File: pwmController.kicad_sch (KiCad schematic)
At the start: 45 parts, among them J1 RJ12, J14 inputs, J16 relays, J17 relays, J2 Conn_01x08_Male, J3 Conn_01x08_Male, J4 Conn_01x08_Male, J5 power, J6 gnd, J7 inputs, J8 track out, K1 G5V-1, K2 G5V-1, K3 G5V-1, K4 G5V-1, K5 G5V-1, K6 G5V-1, K7 G5V-1, K8 G5V-1, U1 24LC256, U2 MAX485E, U3 L298N, U5 ULN2803A, U7 Buck

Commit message: may have the relays working. Should be tested with an LED as soon as the IO extender arrives. Also need to solder pin1 (A0) to 5V due to address conflict with mcp23017
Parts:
- U4: value (none) -> MCP23017_SP; footprint (none) -> Package_DIP:DIP-28_W7.62mm
- U6: value (none) -> PCF8574; footprint (none) -> Package_DIP:DIP-16_W7.62mm_Socket
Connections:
- net +5V: now also U6.1 (A0)
- net GND: no longer U6.1 (A0)
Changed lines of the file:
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@@
   (junction (at 386.08 21.59) (diameter 0) (color 0 0 0 0)
   )
+  (junction (at 250.19 38.1) (diameter 0) (color 0 0 0 0)
+  )
   (junction (at 361.95 160.02) (diameter 0) (color 0 0 0 0)
   )
@@
   )
   (junction (at 71.12 167.64) (diameter 0) (color 0 0 0 0)
-  )
-  (junction (at 232.41 55.88) (diameter 0) (color 0 0 0 0)
   )
   (junction (at 83.82 181.61) (diameter 0) (color 0 0 0 0)
@@
     (stroke (width 0) (type default) (color 0 0 0 0))
   )
+  (wire (pts (xy 232.41 53.34) (xy 232.41 38.1))
+    (stroke (width 0) (type default) (color 0 0 0 0))
+  )
   (wire (pts (xy 35.56 78.74) (xy 40.64 78.74))
     (stroke (width 0) (type default) (color 0 0 0 0))
@@
     (stroke (width 0) (type default) (color 0 0 0 0))
   )
+  (wire (pts (xy 237.49 53.34) (xy 232.41 53.34))
+    (stroke (width 0) (type default) (color 0 0 0 0))
+  )
   (wire (pts (xy 19.05 20.32) (xy 40.64 20.32))
     (stroke (width 0) (type default) (color 0 0 0 0))
@@
     (stroke (width 0) (type default) (color 0 0 0 0))
   )
+  (wire (pts (xy 232.41 38.1) (xy 250.19 38.1))
+    (stroke (width 0) (type default) (color 0 0 0 0))
+  )
   (wire (pts (xy 262.89 53.34) (xy 275.59 53.34))
     (stroke (width 0) (type default) (color 0 0 0 0))
@@
     (stroke (width 0) (type default) (color 0 0 0 0))
   )
-  (wire (pts (xy 232.41 53.34) (xy 232.41 55.88))
-    (stroke (width 0) (type default) (color 0 0 0 0))
-  )
   (wire (pts (xy 167.64 59.69) (xy 167.64 68.58))
     (stroke (width 0) (type default) (color 0 0 0 0))
@@
   )
   (wire (pts (xy 350.52 170.18) (xy 364.49 170.18))
-    (stroke (width 0) (type default) (color 0 0 0 0))
-  )
-  (wire (pts (xy 237.49 53.34) (xy 232.41 53.34))
     (stroke (width 0) (type default) (color 0 0 0 0))
   )
@@
       (effects (font (size 1.27 1.27)) (justify left))
     )
-    (property "Value" "" (id 1) (at 252.2094 39.4771 0)
-      (effects (font (size 1.27 1.27)) (justify left))
-    )
-    (property "Footprint" "" (id 2) (at 250.19 55.88 0)
+    (property "Value" "PCF8574" (id 1) (at 252.2094 39.4771 0)
+      (effects (font (size 1.27 1.27)) (justify left))
+    )
+    (property "Footprint" "Package_DIP:DIP-16_W7.62mm_Socket" (id 2) (at 250.19 55.88 0)
       (effects (font (size 1.27 1.27)) hide)
     )
@@
       (effects (font (size 1.27 1.27)) (justify left))
     )
-    (property "Value" "" (id 1) (at 235.6994 -59.5829 0)
-      (effects (font (size 1.27 1.27)) (justify left))
-    )
-    (property "Footprint" "" (id 2) (at 238.76 -10.16 0)
+    (property "Value" "MCP23017_SP" (id 1) (at 235.6994 -59.5829 0)
+      (effects (font (size 1.27 1.27)) (justify left))
+    )
+    (property "Footprint" "Package_DIP:DIP-28_W7.62mm" (id 2) (at 238.76 -10.16 0)
       (effects (font (size 1.27 1.27)) (justify left) hide)
     )

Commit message: made drastic changes to PCB design. I added 2nd Rj12 connector, side by side connectors, 2 analog inpouts and 2nd channel of H bridge is commissioned
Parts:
- removed J8: track out, TerminalBlock_Phoenix:TerminalBlock_Phoenix_MKDS-1,5-2-5.08_1x02_P5.08mm_Horizontal, symbol Connector:Screw_Terminal_01x02
- removed JP2, JP4: jmp, Jumper:SolderJumper-2_P1.3mm_Open_RoundedPad1.0x1.5mm, symbol Jumper:SolderJumper_2_Open
- added C8, C9: 100nF, Capacitor_THT:C_Disc_D3.0mm_W1.6mm_P2.50mm, symbol Device:C
- added D1, D10, D8, D9: D, Diode_THT:D_DO-34_SOD68_P7.62mm_Horizontal, symbol Device:D
- added J10: Conn_01x06_Female, Connector_PinSocket_2.54mm:PinSocket_1x06_P2.54mm_Horizontal, symbol Connector:Conn_01x06_Female
- added J11, J12: track out, TerminalBlock_Phoenix:TerminalBlock_Phoenix_MKDS-1,5-2-5.08_1x02_P5.08mm_Horizontal, symbol Connector:Screw_Terminal_01x02
- added J13, J15: ADC, Connector_PinHeader_2.54mm:PinHeader_1x03_P2.54mm_Vertical, symbol Connector:Conn_01x03_Male
- added J8: Conn_01x06_Male, Connector_PinHeader_2.54mm:PinHeader_1x06_P2.54mm_Horizontal, symbol Connector:Conn_01x06_Male
- added J9: RJ12, Connector_RJ:RJ12_Amphenol_54601, symbol Connector:RJ12
- added R1: R, Resistor_THT:R_Axial_DIN0516_L15.5mm_D5.0mm_P20.32mm_Horizontal, symbol Device:R
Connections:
- net +12V: now also D3.1 (K), D5.1 (K), D1.1 (K), D9.1 (K), J10.5 (Pin_5), J10.6 (Pin_6), J8.5 (Pin_5), J8.6 (Pin_6), J9.5; no longer D2.1 (K), D4.1 (K), D7.1 (K), U7.4 (in+)
- net +5V: now also U3.11 (EnB), C8.1, C9.1, J13.2 (Pin_2), J15.2 (Pin_2)
- net GND: now also D2.2 (A), D4.2 (A), R2.1, D10.2 (A), D8.2 (A), J10.1 (Pin_1), J10.2 (Pin_2), J13.1 (Pin_1), J15.1 (Pin_1), J8.1 (Pin_1), J8.2 (Pin_2), J9.2, R1.2; no longer D3.2 (A), D5.2 (A), R2.2
- net pwm1: now also A1.13 (D10); no longer A1.19 (A0)
- net pwm2: now also A1.12 (D9); no longer A1.20 (A1)
- net servo7: now also A1.19 (A0); no longer A1.12 (D9)
- net servo8: now also A1.20 (A1); no longer A1.13 (D10)
- net pwm3: now reaches A1.14 (D11)
- net pwm3: now also U3.12 (IN4)
- net pwm4: now reaches A1.15 (D12)
- net pwm4: now also U3.10 (IN3)
- net ADC2: now reaches A1.22 (A3)
- net ADC2: now also C9.2, J13.3 (Pin_3)
- net CS1: now reaches A1.25 (A6)
- net CS1: now also R2.2, U3.1 (SENSE_A)
- net CS2: now reaches A1.26 (A7)
- net CS2: now also U3.15 (SENSE_B), R1.1
- net B: now reaches J1.3, U2.7 (B)
- net B: now also J10.3 (Pin_3), J8.3 (Pin_3), J9.3
- net A: now reaches J1.4, U2.6 (A)
- net A: now also J10.4 (Pin_4), J8.4 (Pin_4), J9.4
- net track2R: now reaches U3.13 (OUT3)
- net track2R: now also D3.2 (A), D4.1 (K), J12.2 (Pin_2)
- net track2L: now reaches U3.14 (OUT4)
- net track2L: now also D10.1 (K), D9.2 (A), J12.1 (Pin_1)
- net coil1_: no longer names the net of U5.8 (I8)
- net coil1_: now also U6.12 (P7); no longer U6.9 (P4)
- net coil2_: no longer names the net of U6.10 (P5)
- net coil2_: now also U5.6 (I6); no longer U5.7 (I7)
- net coil3_: no longer names the net of U6.11 (P6)
- net coil3_: now also U5.7 (I7); no longer U5.6 (I6)
- net coil4_: no longer names the net of U5.5 (I5)
- net coil4_: now also U6.9 (P4); no longer U6.12 (P7)
- net coil5_: no longer names the net of U5.4 (I4), U6.7 (P3)
- net coil6_: no longer names the net of U5.3 (I3), U6.6 (P2)
- net coil7_: no longer names the net of U5.2 (I2), U6.5 (P1)
- net coil8_: no longer names the net of U5.1 (I1), U6.4 (P0)
- net overcurrent renamed ADC1
- net ADC1: now also C8.2, J15.3 (Pin_3)
- removed net rightTrack: D2.2 (A), D3.1 (K), U3.3 (OUT2)
- new net: D7.1 (K), U7.4 (in+)
- new net track1L: D5.2 (A), D8.1 (K), J11.1 (Pin_1), U3.3 (OUT2)
- new net track1R: D1.2 (A), D2.1 (K), J11.2 (Pin_2), U3.2 (OUT1)
- no-connect marks 24 -> 20
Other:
- added sheet EEPROM (EEPROM.kicad_sch)
- added sheet GPIO (GPIO.kicad_sch)
- added sheet H-bridge (H-brigde.kicad_sch)
- added sheet Inputs (Inputs.kicad_sch)
- added sheet interface (interface.kicad_sch)
- added sheet power (power.kicad_sch)
- added sheet relays (relays.kicad_sch)
- added sheet uController (uController.kicad_sch)
- moved on the sheet: C1, C2, C3, C4, C5, C6, C7, D6, D7, J1, J14, J16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

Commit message: divided the schematic in several sheets.
PCB needs to be redrawn because the link between components is gone
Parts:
- removed A1: Arduino_Nano_v3.x, Module:Arduino_Nano, symbol MCU_Module:Arduino_Nano_v3.x
- removed C1, C2, C3, C4, C5, C8, C9: 100nF, Capacitor_THT:C_Disc_D3.0mm_W1.6mm_P2.50mm, symbol Device:C
- removed C6, C7: CP, Capacitor_THT:CP_Radial_D8.0mm_P3.50mm, symbol Device:C_Polarized
- removed D1, D10, D2, D3, D4, D5, D6, D7, D8, D9: D, Diode_THT:D_DO-34_SOD68_P7.62mm_Horizontal, symbol Device:D
- removed J1, J9: RJ12, Connector_RJ:RJ12_Amphenol_54601, symbol Connector:RJ12
- removed J10: Conn_01x06_Female, Connector_PinSocket_2.54mm:PinSocket_1x06_P2.54mm_Horizontal, symbol Connector:Conn_01x06_Female
- removed J11, J12: track out, TerminalBlock_Phoenix:TerminalBlock_Phoenix_MKDS-1,5-2-5.08_1x02_P5.08mm_Horizontal, symbol Connector:Screw_Terminal_01x02
- removed J13, J15: ADC, Connector_PinHeader_2.54mm:PinHeader_1x03_P2.54mm_Vertical, symbol Connector:Conn_01x03_Male
- removed J14, J7: inputs, TerminalBlock_Phoenix:TerminalBlock_Phoenix_MPT-0,5-8-2.54_1x08_P2.54mm_Horizontal, symbol Connector:Screw_Terminal_01x08
- removed J16, J17: relays, TerminalBlock_Phoenix:TerminalBlock_Phoenix_MKDS-1,5-5-5.08_1x05_P5.08mm_Horizontal, symbol Connector:Screw_Terminal_01x05
- removed J2, J3, J4: Conn_01x08_Male, Connector_PinHeader_2.54mm:PinHeader_1x08_P2.54mm_Vertical, symbol Connector:Conn_01x08_Male
- removed J5: power, TerminalBlock_Phoenix:TerminalBlock_Phoenix_MKDS-1,5-2-5.08_1x02_P5.08mm_Horizontal, symbol Connector:Screw_Terminal_01x02
- removed J6: gnd, TerminalBlock_Phoenix:TerminalBlock_Phoenix_MKDS-1,5-2-5.08_1x02_P5.08mm_Horizontal, symbol Connector:Screw_Terminal_01x02
- removed J8: Conn_01x06_Male, Connector_PinHeader_2.54mm:PinHeader_1x06_P2.54mm_Horizontal, symbol Connector:Conn_01x06_Male
- removed JP1, JP3: jmp, Jumper:SolderJumper-2_P1.3mm_Open_RoundedPad1.0x1.5mm, symbol Jumper:SolderJumper_2_Open
- removed K1, K2, K3, K4, K5, K6, K7, K8: G5V-1, Relay_THT:Relay_SPDT_Omron_G5V-1, symbol Relay:G5V-1
- removed R1, R2: R, Resistor_THT:R_Axial_DIN0516_L15.5mm_D5.0mm_P20.32mm_Horizontal, symbol Device:R
- removed U1: 24LC256, Package_DIP:DIP-8_W7.62mm_Socket, symbol Memory_EEPROM:24LC256
- removed U2: MAX485E, Package_DIP:DIP-8_W7.62mm_Socket, symbol Interface_UART:MAX485E
- removed U3: L298N, Package_TO_SOT_THT:TO-220-15_P2.54x2.54mm_StaggerOdd_Lead4.58mm_Vertical, symbol Driver_Motor:L298N
- removed U4: MCP23017_SP, Package_DIP:DIP-28_W7.62mm, symbol Interface_Expansion:MCP23017_SP
- removed U5: ULN2803A, Package_DIP:DIP-18_W7.62mm_Socket, symbol Transistor_Array:ULN2803A
- removed U6: PCF8574, Package_DIP:DIP-16_W7.62mm_Socket, symbol Interface_Expansion:PCF8574
- removed U7: Buck, custom_kicad_lib_sk:Buck, symbol custom_kicad_lib_sk:Buck
- added H1: MountingHole, MountingHole:MountingHole_3.2mm_M3, symbol Mechanical:MountingHole
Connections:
- no-connect marks 20 -> 0
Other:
- title: (none) -> General Purpose IO module

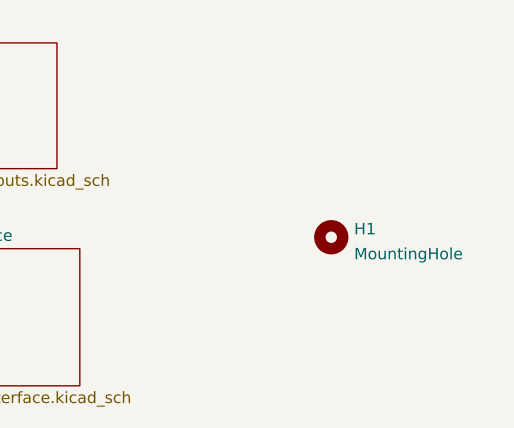
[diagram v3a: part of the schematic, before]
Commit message: changed PCB layout. I want to change more
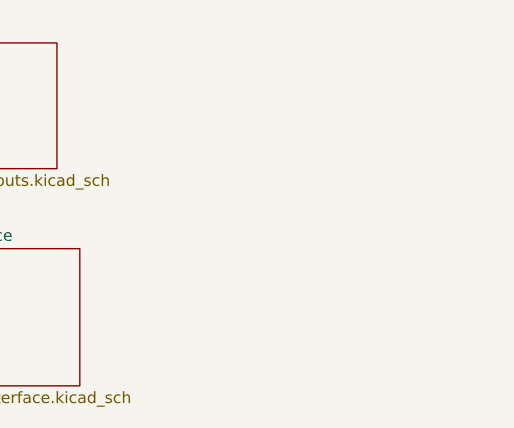
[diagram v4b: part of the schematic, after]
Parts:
- removed H1: MountingHole, MountingHole:MountingHole_3.2mm_M3, symbol Mechanical:MountingHole
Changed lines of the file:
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@@
     (title "General Purpose IO module")
-  )
-  (symbol (lib_id "Mechanical:MountingHole") (at 137.16 40.64 0) (unit 1)
-    (in_bom yes) (on_board yes) (fields_autoplaced)
-    (property "Reference" "H1" (id 0) (at 139.7 39.7315 0)
-      (effects (font (size 1.27 1.27)) (justify left))
-    )
-    (property "Value" "MountingHole" (id 1) (at 139.7 42.5066 0)
-      (effects (font (size 1.27 1.27)) (justify left))
-    )
-    (property "Footprint" "MountingHole:MountingHole_3.2mm_M3" (id 2) (at 137.16 40.64 0)
-      (effects (font (size 1.27 1.27)) hide)
-    )
-    (property "Datasheet" "~" (id 3) (at 137.16 40.64 0)
-      (effects (font (size 1.27 1.27)) hide)
-    )
   )
   (sheet (at 44.45 19.05) (size 15.24 13.97) (fields_autoplaced)
@@
   )
   (symbol_instances
+    (path "/15782add-6e54-4e42-a416-61587f86a435/b3b296ec-345a-438b-88ed-a17ad8ea1576"
+      (reference "#PWR01") (unit 1) (value "+5VA") (footprint "")
+    )
+    (path "/15782add-6e54-4e42-a416-61587f86a435/477facc6-d79a-4dc1-aa3f-86d3bfcca217"
+      (reference "#PWR02") (unit 1) (value "GND") (footprint "")
+    )
+    (path "/15782add-6e54-4e42-a416-61587f86a435/6bf1db2f-8218-4a37-a9ff-28ef9eaeb797"
+      (reference "#PWR03") (unit 1) (value "+5VA") (footprint "")
+    )
+    (path "/15782add-6e54-4e42-a416-61587f86a435/55e2c3cb-7f20-4485-ad3b-1197a660a113"
+      (reference "#PWR04") (unit 1) (value "GND") (footprint "")
+    )
+    (path "/15782add-6e54-4e42-a416-61587f86a435/d1c3fdda-f91d-46b3-8903-4960f9091474"
+      (reference "#PWR05") (unit 1) (value "+5VA") (footprint "")
+    )
+    (path "/15782add-6e54-4e42-a416-61587f86a435/cdb33e69-9124-44b7-8240-f0a2802b2629"
+      (reference "#PWR06") (unit 1) (value "GND") (footprint "")
+    )
+    (path "/15782add-6e54-4e42-a416-61587f86a435/00ee47e2-6951-4070-a450-31f2b1ca61d3"
+      (reference "#PWR07") (unit 1) (value "+5VA") (footprint "")
+    )
+    (path "/15782add-6e54-4e42-a416-61587f86a435/5f987a96-f88c-4c48-9f54-bbb04a7ce0ef"
+      (reference "#PWR08") (unit 1) (value "GND") (footprint "")
+    )
+    (path "/15782add-6e54-4e42-a416-61587f86a435/3acd1d09-7fc9-4a1f-a5a5-37e07d950b90"
+      (reference "#PWR09") (unit 1) (value "+5VA") (footprint "")
+    )
+    (path "/15782add-6e54-4e42-a416-61587f86a435/aefbab52-ffa8-43be-9197-a2369b46f6f8"
+      (reference "#PWR010") (unit 1) (value "GND") (footprint "")
+    )
+    (path "/15782add-6e54-4e42-a416-61587f86a435/6ae46c10-d334-4f3b-8139-fb8860a013fa"
+      (reference "#PWR011") (unit 1) (value "+5VA") (footprint "")
+    )
+    (path "/15782add-6e54-4e42-a416-61587f86a435/78256dce-621e-4a17-8c09-6319ed56b2a8"
+      (reference "#PWR012") (unit 1) (value "GND") (footprint "")
+    )
+    (path "/15782add-6e54-4e42-a416-61587f86a435/c817151f-f542-498d-97f2-d7ebb5b3f4fa"
+      (reference "#PWR013") (unit 1) (value "+5VA") (footprint "")
+    )
+    (path "/15782add-6e54-4e42-a416-61587f86a435/30f5cbe6-e68a-408b-acaf-ef8b43b55fee"
+      (reference "#PWR014") (unit 1) (value "GND") (footprint "")
+    )
+    (path "/15782add-6e54-4e42-a416-61587f86a435/7c34da4a-24eb-4b22-b57e-58032e42e0b1"
+      (reference "#PWR015") (unit 1) (value "+5VA") (footprint "")
+    )
+    (path "/15782add-6e54-4e42-a416-61587f86a435/525a8aee-73cc-4405-b368-88dcce894336"
+      (reference "#PWR016") (unit 1) (value "GND") (footprint "")
+    )
     (path "/5124c4e8-cf6f-404c-8295-c381ef25d08e/8cd7260d-64a2-4a0a-84b1-03181d2c20d1"
       (reference "#PWR0101") (unit 1) (value "GND") (footprint "")
@@
       (reference "#PWR0145") (unit 1) (value "+5V") (footprint "")
     )
-    (path "/15782add-6e54-4e42-a416-61587f86a435/c3c7618f-202a-4b95-b24f-26429b84f4b4"
-      (reference "#PWR0146") (unit 1) (value "GND") (footprint "")
-    )
     (path "/15782add-6e54-4e42-a416-61587f86a435/7a90d089-3f47-41b2-98dc-ed4e9de11862"
       (reference "#PWR0147") (unit 1) (value "GND") (footprint "")
@@
       (reference "#PWR0152") (unit 1) (value "+5V") (footprint "")
     )
-    (path "/15782add-6e54-4e42-a416-61587f86a435/09933ea0-69c3-4150-8976-14f066ab6d37"
-      (reference "#PWR0153") (unit 1) (value "+5VA") (footprint "")
-    )
     (path "/af34ff1d-4916-46f6-b451-19970cdd1d1e/7688b1d7-a5ef-4546-a75a-1dff2b181b93"
       (reference "A1") (unit 1) (value "Arduino_Nano_v3.x") (footprint "Module:Arduino_Nano")
@@
       (reference "D5") (unit 1) (value "D") (footprint "Diode_THT:D_DO-34_SOD68_P7.62mm_Horizontal")
     )
-    (path "/f2e2196a-c83d-497b-b552-0ac27a56ad59/d60723be-0ece-433c-a3cc-8d026e9d4965"
+    (path "/f2e2196a-c83d-497b-b552-0ac27a56ad59/080eb162-2f68-4483-9aa9-cc8e8faf283b"
       (reference "D6") (unit 1) (value "D") (footprint "Diode_THT:D_DO-34_SOD68_P7.62mm_Horizontal")
     )
-    (path "/f2e2196a-c83d-497b-b552-0ac27a56ad59/9f45c2e1-5058-4d3e-94a1-6b3749545d34"
+    (path "/f2e2196a-c83d-497b-b552-0ac27a56ad59/cccb90f6-fcad-4bcc-a6b4-253eb1bab824"
       (reference "D7") (unit 1) (value "D") (footprint "Diode_THT:D_DO-34_SOD68_P7.62mm_Horizontal")
     )
@@
       (reference "D10") (unit 1) (value "D") (footprint "Diode_THT:D_DO-34_SOD68_P7.62mm_Horizontal")
     )
-    (path "/0f730ef4-6b18-4cbd-969a-e0f8ab1030b2"
-      (reference "H1") (unit 1) (value "MountingHole") (footprint "MountingHole:MountingHole_3.2mm_M3")
-    )
     (path "/5124c4e8-cf6f-404c-8295-c381ef25d08e/e63a5e26-dfc1-4721-a4c6-783bbc15c68d"
       (reference "J1") (unit 1) (value "track out") (footprint "TerminalBlock_Phoenix:TerminalBlock_Phoenix_MKDS-1,5-2-5.08_1x02_P5.08mm_Horizontal")
@@
       (reference "J13") (unit 1) (value "ADC") (footprint "Connector_PinHeader_2.54mm:PinHeader_1x03_P2.54mm_Vertical")
     )
-    (path "/15782add-6e54-4e42-a416-61587f86a435/a781526d-7b97-41d9-9f6e-e89d018605de"
-      (reference "J14") (unit 1) (value "Conn_01x08_Male") (footprint "Connector_PinHeader_2.54mm:PinHeader_1x08_P2.54mm_Vertical")
-    )
     (path "/15782add-6e54-4e42-a416-61587f86a435/b24c9c2e-34a1-43da-8250-9a261bf9c0e3"
       (reference "J15") (unit 1) (value "ADC") (footprint "Connector_PinHeader_2.54mm:PinHeader_1x03_P2.54mm_Vertical")
     )
-    (path "/15782add-6e54-4e42-a416-61587f86a435/d4213963-4ff5-490d-a9fa-c018267ae3f9"
-      (reference "J16") (unit 1) (value "Conn_01x08_Male") (footprint "Connector_PinHeader_2.54mm:PinHeader_1x08_P2.54mm_Vertical")
-    )
-    (path "/15782add-6e54-4e42-a416-61587f86a435/632849ab-03e8-4e5b-989b-c97a1a6386f1"
-      (reference "J17") (unit 1) (value "Conn_01x08_Male") (footprint "Connector_PinHeader_2.54mm:PinHeader_1x08_P2.54mm_Vertical")
-    )
     (path "/122d586c-feed-4ee3-99dc-cd90b7ea1328/f0d9f380-a2e8-44a2-961a-18a8c6903b68"
       (reference "JP1") (unit 1) (value "jmp") (footprint "Jumper:SolderJumper-2_P1.3mm_Open_RoundedPad1.0x1.5mm")
@@
       (reference "K8") (unit 1) (value "G5V-1") (footprint "Relay_THT:Relay_SPDT_Omron_G5V-1")
     )
+    (path "/15782add-6e54-4e42-a416-61587f86a435/96179f84-670d-4ff5-93e9-2ff82b7ade81"
+      (reference "M1") (unit 1) (value "Motor_Servo") (footprint "Connector_PinHeader_2.54mm:PinHeader_1x03_P2.54mm_Vertical")
+    )
+    (path "/15782add-6e54-4e42-a416-61587f86a435/07d5c73c-8fc0-4762-b96b-d67536f8bc5f"
+      (reference "M2") (unit 1) (value "Motor_Servo") (footprint "Connector_PinHeader_2.54mm:PinHeader_1x03_P2.54mm_Vertical")
+    )
+    (path "/15782add-6e54-4e42-a416-61587f86a435/295ee17b-2f69-40d1-9fff-dfd5fc46f5e6"
+      (reference "M3") (unit 1) (value "Motor_Servo") (footprint "Connector_PinHeader_2.54mm:PinHeader_1x03_P2.54mm_Vertical")
+    )
+    (path "/15782add-6e54-4e42-a416-61587f86a435/82df33ea-2e2c-428e-945a-d4b9b71f292f"
+      (reference "M4") (unit 1) (value "Motor_Servo") (footprint "Connector_PinHeader_2.54mm:PinHeader_1x03_P2.54mm_Vertical")
+    )
+    (path "/15782add-6e54-4e42-a416-61587f86a435/32ba3a41-7bc5-4813-b947-51b28f879fc1"
+      (reference "M5") (unit 1) (value "Motor_Servo") (footprint "Connector_PinHeader_2.54mm:PinHeader_1x03_P2.54mm_Vertical")
+    )
+    (path "/15782add-6e54-4e42-a416-61587f86a435/4f6890e5-abfa-428c-8da6-9385a5f5738d"
+      (reference "M6") (unit 1) (value "Motor_Servo") (footprint "Connector_PinHeader_2.54mm:PinHeader_1x03_P2.54mm_Vertical")
+    )
+    (path "/15782add-6e54-4e42-a416-61587f86a435/1275069a-78da-4d95-a986-c16be6a6255f"
+      (reference "M7") (unit 1) (value "Motor_Servo") (footprint "Connector_PinHeader_2.54mm:PinHeader_1x03_P2.54mm_Vertical")
+    )
+    (path "/15782add-6e54-4e42-a416-61587f86a435/d4586469-37eb-4eef-9481-91d51749220c"
+      (reference "M8") (unit 1) (value "Motor_Servo") (footprint "Connector_PinHeader_2.54mm:PinHeader_1x03_P2.54mm_Vertical")
+    )
     (path "/5124c4e8-cf6f-404c-8295-c381ef25d08e/043e7a6a-adf2-47fb-ab14-e61c70b46c7a"
